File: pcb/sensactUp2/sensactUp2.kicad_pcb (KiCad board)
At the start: 2 copper layers, 71 x 71 mm, 121 parts, among them J1 SENSACT_BUS, J2 BUS, J3 USB_B_Micro, J4 Conn_01x10, J5 ADAC, J6 1W485, J7 Screw_Terminal_01x02, J8 Conn_01x10, Q1 Q_NPN_BEC, Q2 Q_NPN_BEC, Q3 Q_NPN_BEC, Q4 Q_NPN_BEC, SW1 RotEnc, SW2 Reset, U1 ESP32-WROOM-32D, U10 ADS1115IDGS, U11 STKNX, U2 TPS5430DDA_with_NC, U3 DS2482, U4 SN65HVD230, U5 PCA9555, U6 MAX3485, U7 IPS130-12, U8 MCP4728, U9 LM324

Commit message: Complete reorganisation
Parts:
- removed C21: CFL, Capacitor_SMD:C_0603_1608Metric
- removed C22: CVDDHV, Capacitor_SMD:C_0603_1608Metric
- removed C23: CREF, Capacitor_SMD:C_0603_1608Metric
- removed C24: CFH, Capacitor_SMD:C_0603_1608Metric
- removed C25: CPL, Capacitor_SMD:C_0603_1608Metric
- removed C26: CAC, Capacitor_SMD:C_0603_1608Metric
- removed C27: CGATE, Capacitor_SMD:C_0603_1608Metric
- removed C28: CSS, Capacitor_SMD:C_0603_1608Metric
- removed C29: CFB1, Capacitor_SMD:C_0603_1608Metric
- removed C30: CIN, Capacitor_SMD:C_1206_3216Metric
- removed C31: COUT, Capacitor_SMD:C_1206_3216Metric
- removed D3: D_TVS, Diode_SMD:D_SMC
- removed D4, D5, D6: TS4148RY, Diode_SMD:D_0805_2012Metric
- removed FB1, FB2: FerriteBead, Resistor_SMD:R_1206_3216Metric
- removed J8: Conn_01x10, Connector_PinHeader_2.54mm:PinHeader_1x10_P2.54mm_Vertical
- removed JP1: Jumper, Jumper:SolderJumper-2_P1.3mm_Open_Pad1.0x1.5mm
- removed JP2: Jumper_3_Open, Jumper:SolderJumper-3_P2.0mm_Open_TrianglePad1.0x1.5mm_NumberLabels
- removed L2: L, Inductor_SMD:L_Wuerth_HCI-5040
- removed LS1: Speaker, Buzzer_Beeper:Buzzer_12x9.5RM7.6
- removed Q1, Q2, Q4: Q_NPN_BEC, Package_TO_SOT_SMD:SOT-23
- removed R16, R18, R24, R25, R26, R27, R44: 1k, Resistor_SMD:R_0603_1608Metric
- removed R19: 10k, Resistor_SMD:R_0603_1608Metric
- removed R28, R29, R30, R32, R33, R34, R36, R37, R38, R39, R40, R41, R42, R43: R, Resistor_SMD:R_0603_1608Metric
- removed R31: 3k, Resistor_SMD:R_0603_1608Metric
- removed R35: 12K, Resistor_SMD:R_0603_1608Metric
- removed R45: 10R, Resistor_SMD:R_1206_3216Metric
- removed R46: RDIS, Resistor_SMD:R_0603_1608Metric
- removed R47: RSH, Resistor_SMD:R_0603_1608Metric
- removed R48: RSL, Resistor_SMD:R_0603_1608Metric
- removed R49: RTX, Resistor_SMD:R_2512_6332Metric
- removed R50: RFB2, Resistor_SMD:R_0603_1608Metric
- removed R51: RFB1, Resistor_SMD:R_0603_1608Metric
- removed U10: ADS1115IDGS, Package_SO:TSSOP-10_3x3mm_P0.5mm
- removed U11: STKNX, Package_DFN_QFN:VQFN-24-1EP_4x4mm_P0.5mm_EP2.45x2.45mm_ThermalVias
- removed U6: MAX3485, Package_SO:SOIC-8_3.9x4.9mm_P1.27mm
- removed U7: IPS130-12, WestfaelischeHochschule:IPS130-12
- removed U8: MCP4728, Package_SO:MSOP-10_3x3mm_P0.5mm
- removed U9: LM324, Package_SO:SOIC-14_3.9x8.7mm_P1.27mm
- added IC1: MD8002A, sensact:SOIC-8_3.9x4.9mm_Pitch1.27mm_handsolder, B.Cu at (114.6, 114.3)
- added NT1: Net-Tie_2, NetTie:NetTie-2_SMD_Pad2.0mm, F.Cu at (69.4, 109.5)
- added RV1: 5k, Potentiometer_SMD:Potentiometer_Bourns_3314G_Vertical, F.Cu at (104.8, 118.7)
- added X1: Display_LH154K-PG04, liebler_OPTO:Display_LH154K-PG04, F.Cu at (92.0, 111.0)
- C1: value 10/35V -> 22u; footprint Capacitor_SMD:C_1206_3216Metric -> Capacitor_SMD:C_1206_3216Metric_Pad1.33x1.80mm_HandSolder
- C10, C3, C4, C5: footprint Capacitor_SMD:C_0603_1608Metric -> Capacitor_SMD:C_0805_2012Metric_Pad1.18x1.45mm_HandSolder
- C11: value C -> 10u; footprint Capacitor_SMD:C_0603_1608Metric -> Capacitor_SMD:C_1206_3216Metric_Pad1.33x1.80mm_HandSolder; moved to B.Cu
- C12: value C -> 10u; footprint Capacitor_SMD:C_0603_1608Metric -> Capacitor_SMD:C_1210_3225Metric_Pad1.33x2.70mm_HandSolder
- C13: value u1 -> 10n; footprint Capacitor_SMD:C_0603_1608Metric -> Capacitor_SMD:C_0805_2012Metric_Pad1.18x1.45mm_HandSolder
- C14: value u1 -> m1; footprint Capacitor_SMD:C_0603_1608Metric -> Capacitor_SMD:C_1210_3225Metric_Pad1.33x2.70mm_HandSolder
- C15: value 1u -> m1; footprint Capacitor_SMD:C_0603_1608Metric -> Capacitor_SMD:C_1210_3225Metric_Pad1.33x2.70mm_HandSolder
- C16, C17: value C -> m1; footprint Capacitor_SMD:C_0603_1608Metric -> Capacitor_SMD:C_1210_3225Metric_Pad1.33x2.70mm_HandSolder
- C18: value 1u -> u1; footprint Capacitor_SMD:C_0603_1608Metric -> Capacitor_SMD:C_0805_2012Metric_Pad1.18x1.45mm_HandSolder
- C19: value C -> 10u; footprint Capacitor_SMD:C_0603_1608Metric -> Capacitor_SMD:C_1206_3216Metric_Pad1.33x1.80mm_HandSolder
- C2: value 10u/35V -> u1; footprint Capacitor_SMD:C_1206_3216Metric -> Capacitor_SMD:C_0805_2012Metric_Pad1.18x1.45mm_HandSolder
- C20: value CPH -> 10u; footprint Capacitor_SMD:C_0603_1608Metric -> Capacitor_SMD:C_1206_3216Metric_Pad1.33x1.80mm_HandSolder
- C6: value 10n -> 1u; footprint Capacitor_SMD:C_0603_1608Metric -> Capacitor_SMD:C_0805_2012Metric_Pad1.18x1.45mm_HandSolder; moved to B.Cu
- C7, C8: value 100u/6V3 -> u1; footprint Capacitor_SMD:C_1206_3216Metric -> Capacitor_SMD:C_0805_2012Metric_Pad1.18x1.45mm_HandSolder; moved to B.Cu
- C9: footprint Capacitor_SMD:C_0603_1608Metric -> Capacitor_SMD:C_0805_2012Metric_Pad1.18x1.45mm_HandSolder; moved to B.Cu
- D1: value D_Schottky -> APA-106-F5; footprint Diode_SMD:D_SMA -> LED_THT:LED_D5.0mm-4_RGB
- D2: value LED -> 2A; footprint LED_SMD:LED_2512_6332Metric_Pad1.52x3.35mm_HandSolder -> Diode_SMD:D_SMB_Handsoldering
- J1: value SENSACT_BUS -> PROG; footprint Connector_IDC:IDC-Header_2x05_P2.54mm_Vertical -> liebler_CONN:IDC_2x03_P1.27mm_Vertical; moved to F.Cu
- J3: value USB_B_Micro -> EXT; footprint Connector_USB:USB_Micro-B_Wuerth_614105150721_Vertical -> Connector_Phoenix_MC:PhoenixContact_MCV_1,5_4-G-3.5_1x04_P3.50mm_Vertical; moved to B.Cu
- J4: value Conn_01x10 -> EXT_BUT; footprint Connector_PinHeader_2.54mm:PinHeader_2x05_P2.54mm_Vertical_SMD -> Connector_Phoenix_MC:PhoenixContact_MCV_1,5_8-G-3.5_1x08_P3.50mm_Vertical
- J5: value ADAC -> BUS; footprint Connector_PinHeader_2.54mm:PinHeader_2x05_P2.54mm_Vertical_SMD -> Connector_Phoenix_MC:PhoenixContact_MCV_1,5_4-G-3.5_1x04_P3.50mm_Vertical
- J6: value 1W485 -> 1Wire; footprint Connector_PinHeader_2.54mm:PinHeader_2x02_P2.54mm_Vertical_SMD -> Connector_Phoenix_MC:PhoenixContact_MCV_1,5_2-G-3.5_1x02_P3.50mm_Vertical
- J7: value Screw_Terminal_01x02 -> SPK; footprint Connector_PinSocket_2.54mm:PinSocket_1x02_P2.54mm_Vertical -> Connector_PinHeader_2.54mm:PinHeader_1x02_P2.54mm_Vertical; moved to F.Cu
- L1: footprint Inductor_SMD:L_Wuerth_HCI-7040 -> liebler_PASSIVES:Inductor_CDRH104_handsolder
- Q3: footprint Package_TO_SOT_SMD:SOT-23 -> Package_TO_SOT_SMD:SOT-23_Handsoldering
- R1, R2, R52, R6: footprint Resistor_SMD:R_0603_1608Metric -> Resistor_SMD:R_0805_2012Metric_Pad1.20x1.40mm_HandSolder; moved to B.Cu
- R10: value R -> 10k; footprint Resistor_SMD:R_0603_1608Metric -> Resistor_SMD:R_0805_2012Metric_Pad1.20x1.40mm_HandSolder
- R11: value 10k -> 3k3; footprint Resistor_SMD:R_0603_1608Metric -> Resistor_SMD:R_0805_2012Metric_Pad1.20x1.40mm_HandSolder
- R12, R13, R17, R20, R21, R22, R23, R5, R9: footprint Resistor_SMD:R_0603_1608Metric -> Resistor_SMD:R_0805_2012Metric_Pad1.20x1.40mm_HandSolder
- R14: value 10k -> k1; footprint Resistor_SMD:R_0603_1608Metric -> Resistor_SMD:R_0805_2012Metric_Pad1.20x1.40mm_HandSolder
- R15: value 1k -> 10k; footprint Resistor_SMD:R_0603_1608Metric -> Resistor_SMD:R_0805_2012Metric_Pad1.20x1.40mm_HandSolder; moved to B.Cu
- R3: value 1k -> k1; footprint Resistor_SMD:R_0603_1608Metric -> Resistor_SMD:R_0805_2012Metric_Pad1.20x1.40mm_HandSolder
- R4: value 1k -> k1; footprint Resistor_SMD:R_0603_1608Metric -> Resistor_SMD:R_0805_2012Metric_Pad1.20x1.40mm_HandSolder; moved to F.Cu
- R7: value R -> 10k; footprint Resistor_SMD:R_0603_1608Metric -> Resistor_SMD:R_0805_2012Metric_Pad1.20x1.40mm_HandSolder; moved to B.Cu
- R8: value R -> 22k; footprint Resistor_SMD:R_0603_1608Metric -> Resistor_SMD:R_0805_2012Metric_Pad1.20x1.40mm_HandSolder; moved to B.Cu
- SW1: footprint Rotary_Encoder:RotaryEncoder_Alps_EC11E-Switch_Vertical_H20mm -> smopla:RotaryEncoder_Alps_EC11E-Switch_Vertical_H20mm
- SW2: value Reset -> SW_Push; footprint Button_Switch_SMD:SW_SPST_CK_RS282G05A3 -> sensact:smd_push_handsolder
- U1: value ESP32-WROOM-32D -> ESP32; footprint RF_Module:ESP32-WROOM-32 -> liebler_MODULES:ESP32-WROOM-32_HANDSOLDER
- U2: value TPS5430DDA_with_NC -> TPS5430DDA; footprint Package_SO:TI_SO-PowerPAD-8_ThermalVias -> liebler_SEMICONDUCTORS:SOIC-8_3.9x4.9mm_Pitch1.27mm_pad_handsolder
- U3: footprint Package_SO:SOIC-8_3.9x4.9mm_P1.27mm -> sensact:SOIC-8_3.9x4.9mm_Pitch1.27mm_handsolder; moved to B.Cu
- U4: footprint Package_SO:SOIC-8_3.9x4.9mm_P1.27mm -> sensact:SOIC-8_3.9x4.9mm_Pitch1.27mm_handsolder
- U5: value PCA9555 -> AP1117-33; footprint Package_SO:TSSOP-24_4.4x7.8mm_P0.65mm -> liebler_SEMICONDUCTORS:SOT-223-3_TabPin2_HANDSOLDER; moved to B.Cu
- moved C17 59.1 mm to (83.9, 128.5)
- moved D2 52.7 mm to (90.9, 114.6)
- moved C11 52.3 mm to (112.3, 123.8), turned to 180 degrees
- moved C15 52.2 mm to (88.9, 128.5), turned to 0 degrees
- moved C19 51.3 mm to (103.7, 127.2), turned to 0 degrees
- moved C16 50.3 mm to (71.5, 118.3), turned to 270 degrees
- moved C14 48.3 mm to (71.5, 113.3), turned to 90 degrees
- moved C13 44.1 mm to (87.2, 120.6), turned to 270 degrees
- moved U5 43.6 mm to (104.8, 120.8)
- moved R7 43.6 mm to (120.3, 110.9)
- moved R10 43.5 mm to (86.2, 124.4), turned to 0 degrees
- moved C7 42.9 mm to (118.5, 118.3), turned to 270 degrees
- moved R8 41.7 mm to (118.4, 110.9)
- moved R12 39.8 mm to (93.4, 128.8)
- moved C8 38.4 mm to (114.6, 119.6), turned to 180 degrees
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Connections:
- C1 pad 1: +24V -> +3V3
- C1 pad 2: GND -> GNDD
- C10 pad 2: GND -> GNDD
- C11 pad 2: GND -> GNDD
- C12 pad 1: +3V3 -> +24V
- C13 pad 1: +24V -> /psu/SW
- C13 pad 2: GNDA -> Net-(C13-Pad2)
- C14 pad 1: +3.3VA -> +4V
- C14 pad 2: GNDA -> GND
- C15 pad 1: Net-(C15-Pad1) -> +4V
- C15 pad 2: GNDA -> GND
- C16 pad 1: Net-(C16-Pad1) -> +4V
- C16 pad 2: GNDA -> GND
- C17 pad 1: Net-(C17-Pad1) -> +4V
- C17 pad 2: GNDA -> GND
- C18 pad 2: GNDA -> GNDD
- C19 pad 1: +3.3VA -> +4V
- C19 pad 2: GNDA -> GNDD
- C2 pad 1: +24V -> +3V3
- C2 pad 2: GND -> GNDD
- C20 pad 1: Net-(C20-Pad1) -> +3V3
- C20 pad 2: KNX+ -> GNDD
- C3 pad 1: GND -> GNDD
- C4 pad 2: GND -> GNDD
- C5 pad 1: GND -> GNDD
- C6 pad 2: Net-(C6-Pad2) -> GNDD
- C7 pad 1: +3V3 -> Net-(C7-Pad1)
- C7 pad 2: GND -> Net-(C7-Pad2)
- C8 pad 2: GND -> GNDD
- C9 pad 2: GND -> GNDD
- D1 pad 1: Net-(C6-Pad2) -> Net-(D1-Pad1)
- D1 pad 2: GND -> GNDD
- D2 pad 1: Net-(D2-Pad1) -> /psu/SW
- D2 pad 2: +3V3 -> GND
- J1 pad 1: +3V3 -> EN
- J1 pad 2: EXT_SCL -> +3V3
- J1 pad 3: EXT_SDA -> TXD0
- J1 pad 4: EXT_IRQ0 -> GNDD
- J1 pad 5: EXT_IRQ1 -> RXD0
- J1 pad 6: EXT_IRQ2 -> IO0
- J2 pad 2: GND -> CANH
- J2 pad 3: CANH -> CANL
- J2 pad 4: CANL -> GNDD
- J3 pad 1: RXD0 -> +3V3
- J3 pad 2: DTR -> EXT_SDA
- J3 pad 3: RTS -> EXT_SCL
- J3 pad 4: TXD0 -> GNDD
- J4 pad 1: Net-(J4-Pad1) -> EXT1
- J4 pad 2: Net-(J4-Pad2) -> EXT2
- J4 pad 3: Net-(J4-Pad3) -> EXT3
- J4 pad 4: Net-(J4-Pad4) -> EXT4
- J4 pad 5: Net-(J4-Pad5) -> EXT5
- J4 pad 6: Net-(J4-Pad6) -> EXT6
- J4 pad 7: Net-(J4-Pad7) -> EXT7
- J4 pad 8: Net-(J4-Pad8) -> GNDD
- J5 pad 1: GNDA -> +24V
- J5 pad 2: GNDA -> CANH
- J5 pad 3: /DAC/AIN1 -> CANL
- J5 pad 4: /DAC/AIN3 -> GNDD
- J6 pad 2: GND -> GNDD
- J7 pad 1: KNX+ -> Net-(IC1-Pad5)
- J7 pad 2: KNX- -> Net-(IC1-Pad8)
- L1 pad 1: +3V3 -> +4V
- L1 pad 2: Net-(C6-Pad2) -> /psu/SW
- Q3 pad 2: GND -> GNDD
- R10 pad 1: Net-(LS1-Pad1) -> +4V
- R10 pad 2: SPK_OUT -> /psu/VSENSE
- R11 pad 1: EN -> /psu/VSENSE
- R11 pad 2: +3V3 -> Net-(R11-Pad2)
- R12 pad 1: Net-(R12-Pad1) -> Net-(R11-Pad2)
- R12 pad 2: EN -> GND
- R14 pad 1: DTR -> EN
- R14 pad 2: Net-(Q2-Pad1) -> Net-(C18-Pad1)
- R15 pad 2: EXT_IRQ0 -> EN
- R52 pad 2: GND -> GNDD
- R7 pad 1: +3V3 -> Net-(IC1-Pad4)
- R7 pad 2: Net-(R7-Pad2) -> Net-(C7-Pad1)
- R8 pad 1: Net-(R7-Pad2) -> Net-(IC1-Pad5)
- R8 pad 2: GND -> Net-(IC1-Pad4)
- R9 pad 2: GND -> GNDD
- SW1 pad C: GND -> GNDD
- SW1 pad S2: +3V3 -> GNDD
- SW2 pad 1: Net-(R12-Pad1) -> GNDD
- SW2 pad 2: GND -> EN
- U1 pad 1: GND -> GNDD
- U1 pad 11: EXT_SCL -> LCD_CLK
- U1 pad 13: LCD_CLK -> LCD_BL
- U1 pad 14: LCD_RES -> LED
- U1 pad 15: GND -> GNDD
- U1 pad 16: LCD_MOSI -> Net-(U1-Pad16)
- U1 pad 17: (no net) -> Net-(U1-Pad17)
- U1 pad 18: (no net) -> Net-(U1-Pad18)
- U1 pad 19: (no net) -> Net-(U1-Pad19)
- U1 pad 20: (no net) -> Net-(U1-Pad20)
- U1 pad 21: (no net) -> Net-(U1-Pad21)
- U1 pad 22: (no net) -> Net-(U1-Pad22)
- U1 pad 23: KNX_TX -> Net-(U1-Pad23)
- U1 pad 24: LCD_BL -> CANT
- U1 pad 26: Net-(JP2-Pad2) -> EXT_SCL
- U1 pad 27: CANR -> EXT_SDA
- U1 pad 28: RS485_DE -> EXT3
- U1 pad 29: RS485_DI -> EXT4
- U1 pad 30: IO_IRQ -> EXT5
- U1 pad 31: RS485_RO -> EXT6
- U1 pad 32: (no net) -> Net-(U1-Pad32)
- U1 pad 36: I2C_SCL -> EXT7
- U1 pad 37: /LED -> I2C_SCL
- U1 pad 38: GND -> GNDD
- U1 pad 39: (no net) -> GNDD
- U1 pad 6: EXT_IRQ2 -> Net-(U1-Pad6)
- U1 pad 7: EXT_IRQ1 -> CANR
- U1 pad 8: EXT_IRQ0 -> LCD_RES
- U1 pad 9: EXT_SDA -> LCD_MOSI
- U2 pad 1: Net-(C6-Pad1) -> Net-(C13-Pad2)
- U2 pad 2: GND -> Net-(U2-Pad2)
- U2 pad 3: GND -> Net-(U2-Pad3)
- U2 pad 4: Net-(R7-Pad2) -> /psu/VSENSE
- U2 pad 5: (no net) -> +24V
- U2 pad 8: Net-(C6-Pad2) -> /psu/SW
- U3 pad 3: GND -> GNDD
- U3 pad 6: (no net) -> Net-(U3-Pad6)
- U3 pad 7: GND -> GNDD
- U3 pad 8: GND -> GNDD
- U4 pad 2: GND -> GNDD
- U4 pad 5: (no net) -> Net-(U4-Pad5)
- U5 pad 1: IO_IRQ -> GNDD
- U5 pad 2: GND -> +3V3
- U5 pad 3: GND -> +4V
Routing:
- net +3V3: track 314.9 -> 163.3 mm, vias 8 -> 3
- net GND: track 122.0 -> 7.69 mm, vias 154 -> 1
- net KNX_KNXOK: track 95.5 -> 0.00 mm, vias 3 -> 0
- net +4V: track 0.00 -> 69.4 mm, vias 0 -> 2
- net GNDA: track 65.1 -> 0.00 mm, vias 36 -> 0
- net KNX_TX: track 61.1 -> 0.00 mm, vias 3 -> 0
- net EN: track 44.0 -> 100.2 mm
- net KNX_RX: track 54.4 -> 0.00 mm, vias 3 -> 0
- net +24V: track 72.1 -> 22.2 mm, vias 0 -> 3
- net 1W: track 6.87 -> 47.3 mm
- net Net-(R42-Pad2): track 37.4 -> 0.00 mm
- net GNDD: track 0.00 -> 37.1 mm, vias 0 -> 6
- net EXT_IRQ2: track 36.7 -> 0.00 mm
- net +3.3VA: track 34.9 -> 0.00 mm, vias 1 -> 0
- net EXT_IRQ1: track 34.8 -> 0.00 mm
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- added copper zone on F.Cu, net /psu/SW
- added copper zone on B.Cu, net GNDD
- added copper zone on F.Cu, net GNDD
- removed copper zone on B.Cu, net GND
- removed copper zone on B.Cu, net GNDA
- removed copper zone on F.Cu, net GNDA
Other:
- outline, holes or cut-outs redrawn
- net class Default: clearance 0.1905 -> 0.199; trace_width 0.2032 -> 0.2; via_dia 0.7 -> 0.6
- net class HighVoltage: clearance 0.254 -> 0.299; trace_width 0.2032 -> 0.2; via_dia 0.7 -> 0.6
- rule trace_clearance: 0.1905 -> 0.199
- rule via_min_size: 0.7 -> 0.6

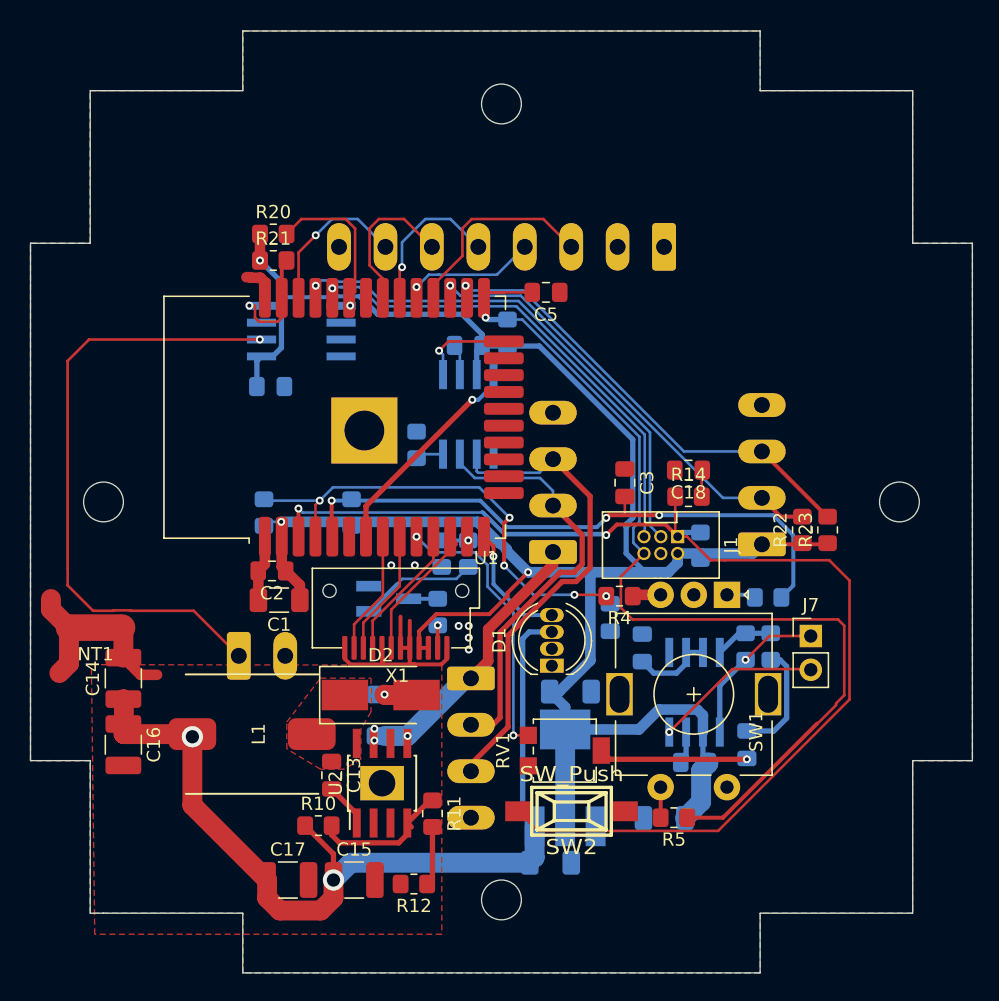
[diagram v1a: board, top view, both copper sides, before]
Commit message: sensactUP2, sensactHsNano sensactHsLED sensactOutdoor as ordered at JLCPCB
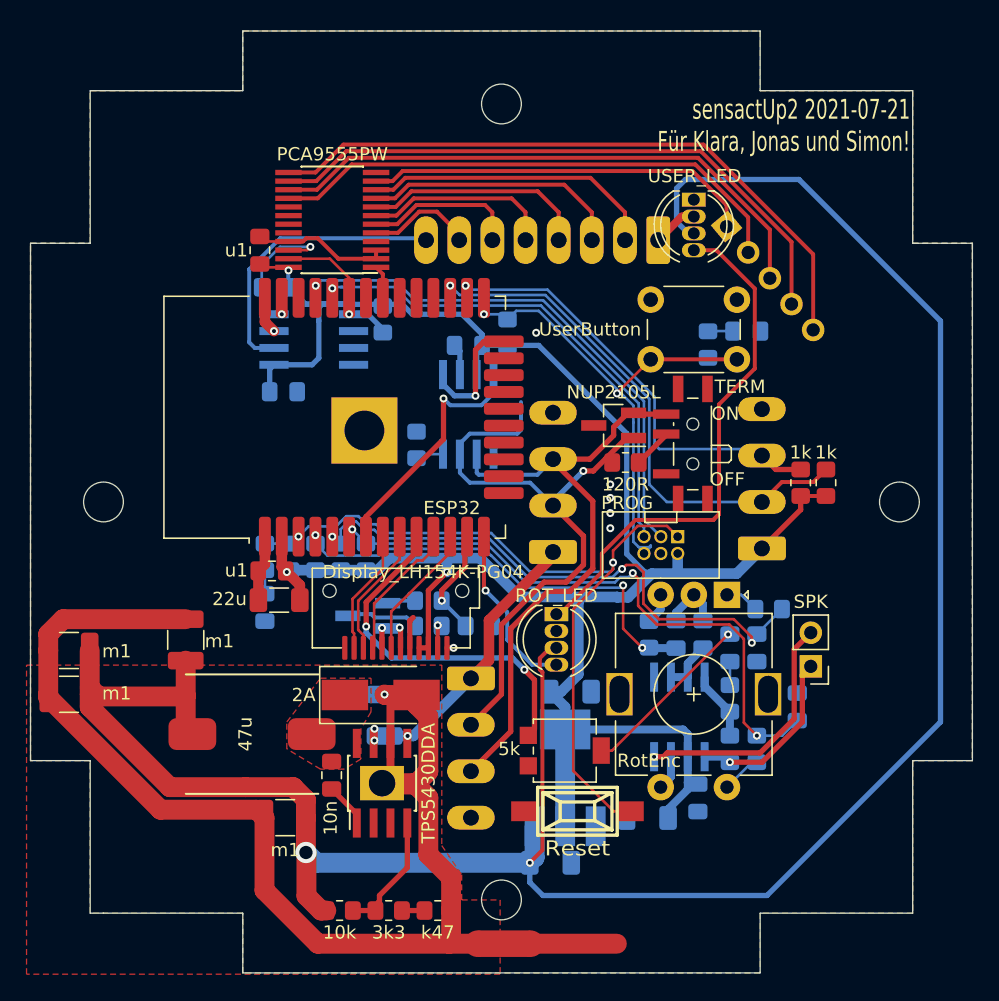
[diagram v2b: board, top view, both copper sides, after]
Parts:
- added C21: u1, Capacitor_SMD:C_0805_2012Metric_Pad1.18x1.45mm_HandSolder, B.Cu at (118.5, 87.1)
- added C22: u1, Capacitor_SMD:C_0805_2012Metric_Pad1.18x1.45mm_HandSolder, F.Cu at (81.8, 81.0)
- added D3: USER_LED, LED_THT:LED_D5.0mm-4_RGB, F.Cu at (114.5, 77.2)
- added D4: NUP2105L, Package_TO_SOT_SMD:SOT-23_Handsoldering, F.Cu at (108.5, 94.2)
- added R16: k1, Resistor_SMD:R_0805_2012Metric_Pad1.20x1.40mm_HandSolder, B.Cu at (115.6, 88.1)
- added R18: 10k, Resistor_SMD:R_0805_2012Metric_Pad1.20x1.40mm_HandSolder, B.Cu at (100.5, 87.2)
- added R19: 120R, Resistor_SMD:R_0805_2012Metric_Pad1.20x1.40mm_HandSolder, F.Cu at (109.3, 97.0)
- added SW3: UserButton, Button_Switch_THT:SW_PUSH_6mm_H13mm, F.Cu at (114.5, 87.0)
- added SW4: TERM, liebler_MECH:SW_SPDT_PCM12_handsolder, F.Cu at (114.1, 95.6)
- added U6: PCA9555PW, liebler_SEMICONDUCTORS:TSSOP-24_4.4x7.8mm_Pitch0.65mm_handsolder, F.Cu at (87.2, 78.7)
- C18, C3, C5, R14, R20, R21, R4, R5: moved to B.Cu
- D1: value APA-106-F5 -> ROT_LED
- J2: value BUS -> GND CL CH 24V
- J3: value EXT -> GND SCL SDA 3V3
- J4: value EXT_BUT -> GND EXT1...EXT16 1W; footprint Connector_Phoenix_MC:PhoenixContact_MCV_1,5_8-G-3.5_1x08_P3.50mm_Vertical -> liebler_CONN:PhoenixContact_MCV_0,5_8-G-2.5_1x08_P2.50mm_vertical
- J5: value BUS -> 24V CH CL GND
- J6: value 1Wire -> EXT 11...7; footprint Connector_Phoenix_MC:PhoenixContact_MCV_1,5_2-G-3.5_1x02_P3.50mm_Vertical -> Connector_PinHeader_2.54mm:PinHeader_1x05_P2.54mm_Vertical
- SW2: value SW_Push -> Reset
- moved J6 49.0 mm to (117.0, 79.2), turned to 220 degrees
- moved NT1 38.9 mm to (100.2, 133.3), turned to 0 degrees
- moved C5 36.5 mm to (122.3, 115.4), turned to 270 degrees
- moved C18 33.6 mm to (82.2, 108.0), turned to 270 degrees
- moved R14 32.3 mm to (82.2, 104.1), turned to 270 degrees
- moved R15 30.9 mm to (84.1, 104.1)
- moved C15 27.6 mm to (67.4, 111.2), turned to 180 degrees
- moved R6 20.0 mm to (89.8, 104.1)
- moved C17 19.7 mm to (76.2, 110.4), turned to 90 degrees
- moved C14 16.1 mm to (83.7, 123.8), turned to 180 degrees
- moved C3 15.9 mm to (119.3, 111.0), turned to 90 degrees
- moved R20 10.5 mm to (91.1, 86.2), turned to 270 degrees
- moved R5 8.12 mm to (119.3, 118.6), turned to 270 degrees
- moved R11 8.01 mm to (91.5, 130.8), turned to 0 degrees
- moved R8 7.81 mm to (117.2, 118.6)
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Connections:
- C5 pad 2: IO0 -> ROT1_S
- J4 pad 1: EXT1 -> GNDD
- J4 pad 2: EXT2 -> EXT1
- J4 pad 3: EXT3 -> EXT2
- J4 pad 4: EXT4 -> EXT3
- J4 pad 5: EXT5 -> EXT4
- J4 pad 6: EXT6 -> EXT5
- J4 pad 7: EXT7 -> EXT6
- J4 pad 8: GNDD -> 1W
- J6 pad 1: 1W -> EXT7
- J6 pad 2: GNDD -> EXT8
- R5 pad 1: IO0 -> ROT1_S
- R6 pad 2: IO0 -> ROT1_S
- SW1 pad S1: Net-(R5-Pad2) -> GNDD
- SW1 pad S2: GNDD -> Net-(R5-Pad2)
- U1 pad 28: EXT3 -> Net-(U1-Pad28)
- U1 pad 29: EXT4 -> Net-(U1-Pad29)
- U1 pad 30: EXT5 -> Net-(U1-Pad30)
- U1 pad 31: EXT6 -> PCA_INT
- U1 pad 36: EXT7 -> Net-(U1-Pad36)
- U1 pad 6: Net-(U1-Pad6) -> ROT1_S
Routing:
- net +4V: track 69.4 -> 181.6 mm
- net GND: track 7.69 -> 94.2 mm
- net EXT11: track 0.00 -> 49.5 mm
- net EXT10: track 0.00 -> 46.4 mm
- net ROT1_S: track 0.00 -> 46.0 mm, vias 0 -> 3
- net EXT9: track 0.00 -> 43.2 mm
- net Net-(D1-Pad1): track 0.00 -> 42.7 mm
- net EN: track 100.2 -> 59.0 mm
- net EXT8: track 0.00 -> 40.0 mm
- net IO0: track 74.3 -> 39.8 mm, vias 1 -> 2
- net 1W: track 47.3 -> 21.9 mm, vias 1 -> 0
- net EXT1: track 0.00 -> 22.3 mm
- net EXT2: track 0.00 -> 19.7 mm
- net EXT7: track 11.9 -> 29.4 mm, vias 1 -> 0
- net CANH: track 32.2 -> 48.3 mm, vias 0 -> 1
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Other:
- board text added: "OFF"
- board text added: "ON"
- board text added: "sensactUp2 2021-07-21 Für Klara, Jonas und Simon!"

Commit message: sensactHsNano for Reflow Soldering
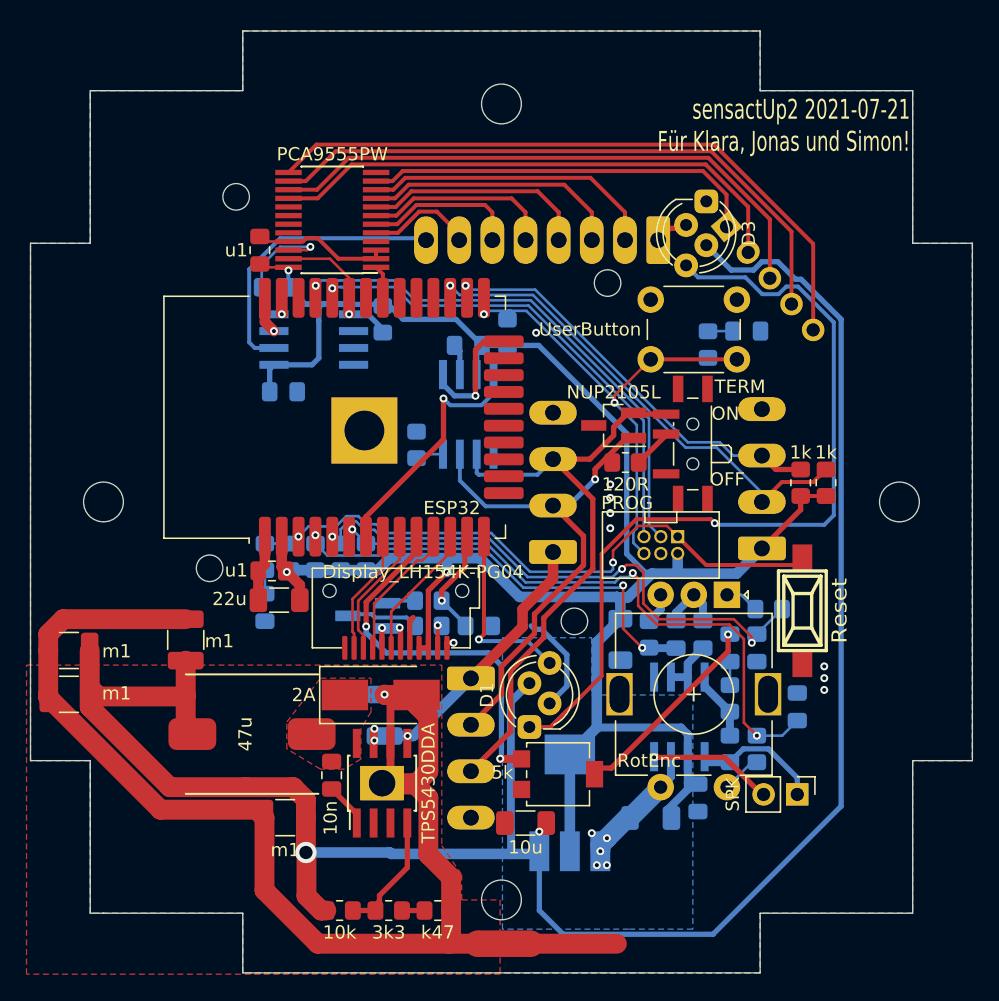
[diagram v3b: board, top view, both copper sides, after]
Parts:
- C19: moved to F.Cu
- D1, D3: footprint LED_THT:LED_D5.0mm-4_RGB -> LED_THT:LED_D5.0mm-4_RGB_Staggered_Pins
- R5: value 1k -> k1
- moved SW2 22.7 mm to (122.7, 108.2), turned to 90 degrees
- moved J7 9.71 mm to (122.3, 122.0), turned to 270 degrees
- moved D1 8.75 mm to (102.1, 117.0), turned to 90 degrees
- moved C20 5.45 mm to (109.0, 110.4), turned to 270 degrees
- moved C19 3.54 mm to (101.8, 124.2), turned to 180 degrees
- moved U5 1.92 mm to (105.2, 122.7)
- moved RV1 1.85 mm to (104.3, 120.5)
- moved D3 0.95 mm to (115.4, 77.3)
- moved C11 0.25 mm to (111.3, 123.8)
- turned C4 to 270 degrees
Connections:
- C4 pad 1: ROT1_B -> GNDD
- C4 pad 2: GNDD -> ROT1_B
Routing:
- net Net-(D1-Pad1): track 42.7 -> 64.9 mm, vias 0 -> 1
- net +4V: track 181.6 -> 160.9 mm
- net GNDD: track 43.7 -> 57.8 mm, vias 9 -> 17
- net EN: track 59.0 -> 47.0 mm
- net Net-(IC1-Pad8): track 18.8 -> 9.46 mm
- net CANH: track 48.3 -> 40.1 mm
- net Net-(IC1-Pad5): track 13.2 -> 9.72 mm, vias 1 -> 0
- net EXT_SDA: track 39.9 -> 36.5 mm
- net EXT_SCL: track 33.1 -> 31.1 mm
- net Net-(C7-Pad2): track 13.3 -> 15.1 mm
- net SPK_OUT: track 27.4 -> 28.7 mm
- net +3V3: track 162.8 -> 161.5 mm
- net LED: track 13.0 -> 14.0 mm
- net CANL: track 47.6 -> 46.7 mm
- net +24V: track 22.7 -> 21.8 mm
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- added copper zone on B.Cu, net +3V3
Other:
- outline, holes or cut-outs redrawn

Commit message: sensactUP3 and sensactUPUpdates to KiCad6
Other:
- net class Default removed
- net class HighVoltage removed
